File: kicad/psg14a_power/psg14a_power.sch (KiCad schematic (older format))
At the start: 5 parts

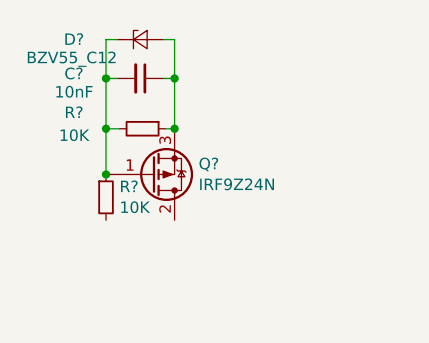
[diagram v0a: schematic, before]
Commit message: [psg14a_power]Schematics finished
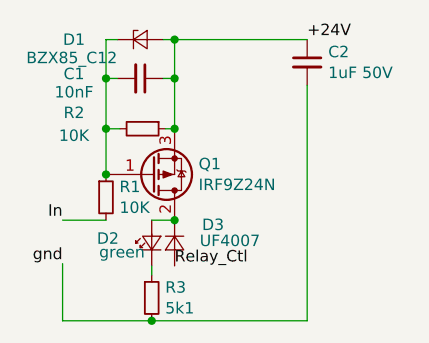
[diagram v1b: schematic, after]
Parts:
- added C2: 1uF 50V, Capacitors_SMD:C_0805_HandSoldering, symbol Device:C_Small
- added D2: green, LEDs:LED_0805_HandSoldering, symbol Device:LED_Small
- added D3: UF4007, Diodes_THT:D_DO-41_SOD81_P5.08mm_Vertical_AnodeUp, symbol Device:D_Small
- added R3: 5k1, Resistors_SMD:R_0805_HandSoldering, symbol Device:R_Small
- C1: renamed from C?; footprint (none) -> Capacitors_SMD:C_0805_HandSoldering
- D1: renamed from D?; value BZV55_C12 -> BZX85_C12; footprint (none) -> Diodes_THT:D_DO-41_SOD81_P5.08mm_Vertical_AnodeUp
- Q1: renamed from Q?; footprint Package_TO_SOT_THT:TO-220-3_Vertical -> TO_SOT_Packages_THT:TO-220-3_Vertical
- R1, R2: renamed from R?; footprint (none) -> Resistors_SMD:R_0805_HandSoldering
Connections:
- net at Q1.2 (D): now also D2.2 (A), D3.1 (K)
- net +24V: now reaches C1.1, D1.2 (A), Q1.3 (S), R2.1
- net +24V: now also C2.1
- net In: now reaches R1.2
- new net: D2.1 (K), R3.1
- new net Relay_Ctl: D3.2 (A)
- new net gnd: C2.2, R3.2
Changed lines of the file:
@@
 EESchema Schematic File Version 4
+LIBS:psg14a_power-cache
 EELAYER 26 0
 EELAYER END
@@
 $EndDescr
 $Comp
-L Transistor_FET:IRF9540N Q?
+L Transistor_FET:IRF9540N Q1
 U 1 1 5C02A0F2
 P 2450 1430
-F 0 "Q?" H 2655 1384 50  0000 L CNN
+F 0 "Q1" H 2655 1384 50  0000 L CNN
 F 1 "IRF9Z24N" H 2655 1475 50  0000 L CNN
-F 2 "Package_TO_SOT_THT:TO-220-3_Vertical" H 2650 1355 50  0001 L CIN
+F 2 "TO_SOT_Packages_THT:TO-220-3_Vertical" H 2650 1355 50  0001 L CIN
 F 3 "http://www.irf.com/product-info/datasheets/data/irf9540n.pdf" H 2450 1430 50  0001 L CNN
 	1    2450 1430
@@
 $EndComp
 $Comp
-L Device:R_Small R?
+L Device:R_Small R1
 U 1 1 5C02A204
 P 2250 1530
-F 0 "R?" H 2309 1576 50  0000 L CNN
+F 0 "R1" H 2309 1576 50  0000 L CNN
 F 1 "10K" H 2309 1485 50  0000 L CNN
-F 2 "" H 2250 1530 50  0001 C CNN
+F 2 "Resistors_SMD:R_0805_HandSoldering" H 2250 1530 50  0001 C CNN
 F 3 "~" H 2250 1530 50  0001 C CNN
 	1    2250 1530
@@
 $EndComp
 $Comp
-L Device:R_Small R?
+L Device:R_Small R2
 U 1 1 5C02A2A6
 P 2410 1230
-F 0 "R?" V 2340 930 50  0000 C CNN
+F 0 "R2" V 2340 930 50  0000 C CNN
 F 1 "10K" V 2440 930 50  0000 C CNN
-F 2 "" H 2410 1230 50  0001 C CNN
+F 2 "Resistors_SMD:R_0805_HandSoldering" H 2410 1230 50  0001 C CNN
 F 3 "~" H 2410 1230 50  0001 C CNN
 	1    2410 1230
@@
 Connection ~ 2250 1430
 $Comp
-L Device:C_Small C?
+L Device:C_Small C1
 U 1 1 5C02A3CA
 P 2400 1010
-F 0 "C?" V 2380 720 50  0000 C CNN
+F 0 "C1" V 2380 720 50  0000 C CNN
 F 1 "10nF" V 2460 720 50  0000 C CNN
-F 2 "" H 2400 1010 50  0001 C CNN
+F 2 "Capacitors_SMD:C_0805_HandSoldering" H 2400 1010 50  0001 C CNN
 F 3 "~" H 2400 1010 50  0001 C CNN
 	1    2400 1010
@@
 $EndComp
 $Comp
-L Device:D_Zener_Small D?
+L Device:D_Zener_Small D1
 U 1 1 5C02A910
 P 2400 840
-F 0 "D?" H 2110 840 50  0000 C CNN
-F 1 "BZV55_C12" H 2100 760 50  0000 C CNN
-F 2 "" V 2400 840 50  0001 C CNN
+F 0 "D1" H 2110 840 50  0000 C CNN
+F 1 "BZX85_C12" H 2100 760 50  0000 C CNN
+F 2 "Diodes_THT:D_DO-41_SOD81_P5.08mm_Vertical_AnodeUp" V 2400 840 50  0001 C CNN
 F 3 "~" V 2400 840 50  0001 C CNN
 	1    2400 840
@@
 Wire Wire Line
 	2250 1230 2250 1430
+Wire Wire Line
+	2250 1630 2060 1630
+Text Label 2060 1630 2    50   ~ 0
+In
+$Comp
+L Device:D_Small D3
+U 1 1 5C0EF074
+P 2550 1730
+F 0 "D3" V 2470 1850 50  0000 L CNN
+F 1 "UF4007" V 2540 1840 50  0000 L CNN
+F 2 "Diodes_THT:D_DO-41_SOD81_P5.08mm_Vertical_AnodeUp" V 2550 1730 50  0001 C CNN
+F 3 "~" V 2550 1730 50  0001 C CNN
+	1    2550 1730
+	0    1    1    0
+$EndComp
+Wire Wire Line
+	2550 1630 2450 1630
+$Comp
+L Device:LED_Small D2
+U 1 1 5C0EF3AD
+P 2450 1730
+F 0 "D2" V 2470 1970 50  0000 R CNN
+F 1 "green" V 2410 1960 50  0000 R CNN
+F 2 "LEDs:LED_0805_HandSoldering" V 2450 1730 50  0001 C CNN
+F 3 "~" V 2450 1730 50  0001 C CNN
+	1    2450 1730
+	0    -1   -1   0
+$EndComp
+Connection ~ 2550 1630
+$Comp
+L Device:R_Small R3
+U 1 1 5C0EF5C4
+P 2450 1970
+F 0 "R3" H 2509 2016 50  0000 L CNN
+F 1 "5k1" H 2509 1925 50  0000 L CNN
+F 2 "Resistors_SMD:R_0805_HandSoldering" H 2450 1970 50  0001 C CNN
+F 3 "~" H 2450 1970 50  0001 C CNN
+	1    2450 1970
+	1    0    0    -1
+$EndComp
+Wire Wire Line
+	2450 1830 2450 1870
+Text Label 2550 1830 0    50   ~ 0
+Relay_Ctl
+Wire Wire Line
+	2060 1820 2060 2070
+Wire Wire Line
+	2060 2070 2450 2070
+Connection ~ 2450 2070
+Wire Wire Line
+	2450 2070 3130 2070
+$Comp
+L Device:C_Small C2
+U 1 1 5C0EFE1A
+P 3130 940
+F 0 "C2" H 3222 986 50  0000 L CNN
+F 1 "1uF 50V" H 3222 895 50  0000 L CNN
+F 2 "Capacitors_SMD:C_0805_HandSoldering" H 3130 940 50  0001 C CNN
+F 3 "~" H 3130 940 50  0001 C CNN
+	1    3130 940
+	1    0    0    -1
+$EndComp
+Wire Wire Line
+	3130 1040 3130 2070
+Wire Wire Line
+	3130 840  2550 840
+Connection ~ 2550 840
+Text Label 2060 1820 2    50   ~ 0
+gnd
+Text Label 3130 840  0    50   ~ 0
++24V
 $EndSCHEMATC

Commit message: [psg14a] looking how to copy blocks
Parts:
- added C10, C5, C6, C8: 1uF 50V, Capacitors_SMD:C_0805_HandSoldering, symbol Device:C_Small
- added C3, C4, C7, C9: 10nF, Capacitors_SMD:C_0805_HandSoldering, symbol Device:C_Small
- added D10, D13, D4, D5: BZX85_C12, Diodes_THT:D_DO-41_SOD81_P5.08mm_Vertical_AnodeUp, symbol Device:D_Zener_Small
- added D11, D14, D6, D7: green, LEDs:LED_0805_HandSoldering, symbol Device:LED_Small
- added D12, D15, D8, D9: UF4007, Diodes_THT:D_DO-41_SOD81_P5.08mm_Vertical_AnodeUp, symbol Device:D_Small
- added Q2, Q3, Q4, Q5: IRF9Z24N, TO_SOT_Packages_THT:TO-220-3_Vertical, symbol Transistor_FET:IRF9540N
- added R10, R11, R13, R14, R4, R5, R6, R8: 10K, Resistors_SMD:R_0805_HandSoldering, symbol Device:R_Small
- added R12, R15, R7, R9: 5k1, Resistors_SMD:R_0805_HandSoldering, symbol Device:R_Small
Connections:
- net +24V: now also C10.1, C3.1, C4.1, C5.1, C6.1, C7.1, C8.1, C9.1, D10.2 (A), D13.2 (A), D4.2 (A), D5.2 (A), Q2.3 (S), Q3.3 (S), Q4.3 (S), Q5.3 (S), R11.1, R14.1, R6.1, R8.1
- net In: now also R10.2, R13.2, R4.2, R5.2
- net Relay_Ctl: now also D2.2 (A), D3.1 (K), Q1.2 (D), D11.2 (A), D12.1 (K), D14.2 (A), D15.1 (K), D6.2 (A), D7.2 (A), D8.1 (K), D9.1 (K), Q2.2 (D), Q3.2 (D), Q4.2 (D), Q5.2 (D); no longer D3.2 (A)
- net gnd: now also C10.2, C5.2, C6.2, C8.2, D12.2 (A), D8.2 (A), D9.2 (A), R12.2, R15.2, R7.2, R9.2
- new net: C9.2, D13.1 (K), Q5.1 (G), R13.1, R14.2
- new net: D14.1 (K), R15.1
- new net: C3.2, D4.1 (K), Q2.1 (G), R4.1, R6.2
- new net: D6.1 (K), R7.1
- new net: C4.2, D5.1 (K), Q3.1 (G), R5.1, R8.2
- new net: D7.1 (K), R9.1
- new net: C7.2, D10.1 (K), Q4.1 (G), R10.1, R11.2
- new net: D11.1 (K), R12.1

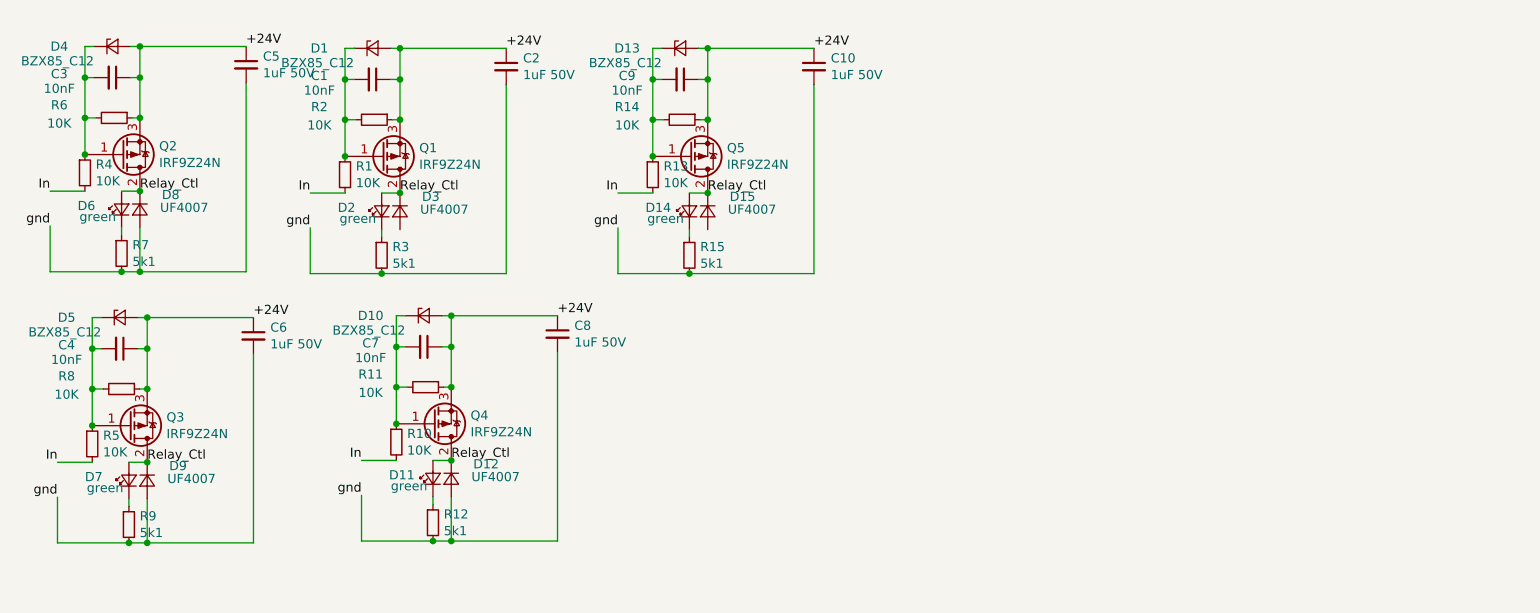
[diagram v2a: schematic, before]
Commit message: [psg14a_power]New route added
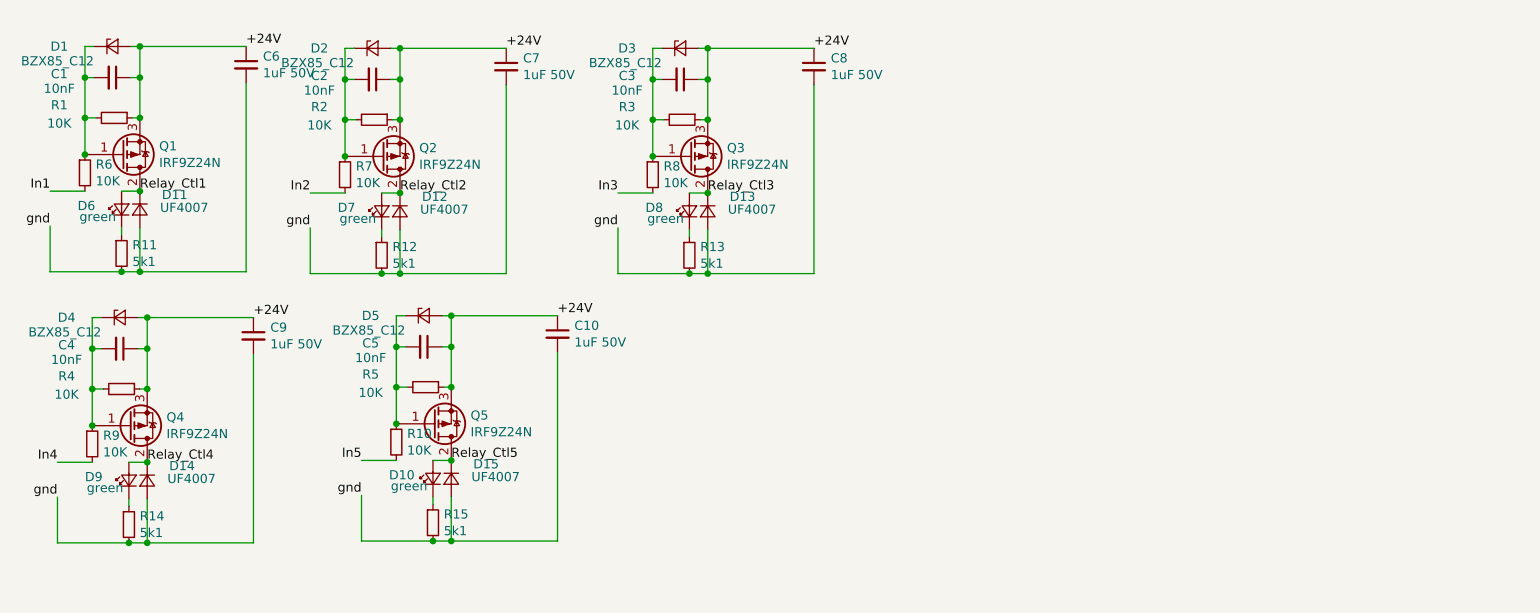
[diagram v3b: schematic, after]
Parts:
- renumbered C3 to C1, C8 to C10, C1 to C2, C9 to C3, C7 to C5, C5 to C6, C2 to C7, C10 to C8, C6 to C9, D4 to D1, D11 to D10, D8 to D11, D3 to D12, D15 to D13, D9 to D14, D12 to D15, D1 to D2, D13 to D3, D5 to D4, D10 to D5, D2 to D7, D14 to D8, D7 to D9, Q2 to Q1, Q1 to Q2, Q5 to Q3, Q3 to Q4, Q4 to Q5, R6 to R1, R7 to R11, R3 to R12, R15 to R13, R9 to R14, R12 to R15, R14 to R3, R8 to R4, R11 to R5, R4 to R6, R1 to R7, R13 to R8, R5 to R9
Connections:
- net gnd: now also D12.2 (A), D13.2 (A)
- removed net In: R10.2, R6.2, R7.2, R8.2, R9.2
- removed net Relay_Ctl: D10.2 (A), D11.1 (K), D12.1 (K), D13.1 (K), D14.1 (K), D15.1 (K), D6.2 (A), D7.2 (A), D8.2 (A), D9.2 (A), Q1.2 (D), Q2.2 (D), Q3.2 (D), Q4.2 (D), Q5.2 (D)
- new net In1: R6.2
- new net In2: R7.2
- new net In3: R8.2
- new net In4: R9.2
- new net In5: R10.2
- new net Relay_Ctl1: D11.1 (K), D6.2 (A), Q1.2 (D)
- new net Relay_Ctl2: D12.1 (K), D7.2 (A), Q2.2 (D)
- new net Relay_Ctl3: D13.1 (K), D8.2 (A), Q3.2 (D)
- new net Relay_Ctl4: D14.1 (K), D9.2 (A), Q4.2 (D)
- new net Relay_Ctl5: D10.2 (A), D15.1 (K), Q5.2 (D)

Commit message: [psg14a_power] Switch to multiple sheets layout
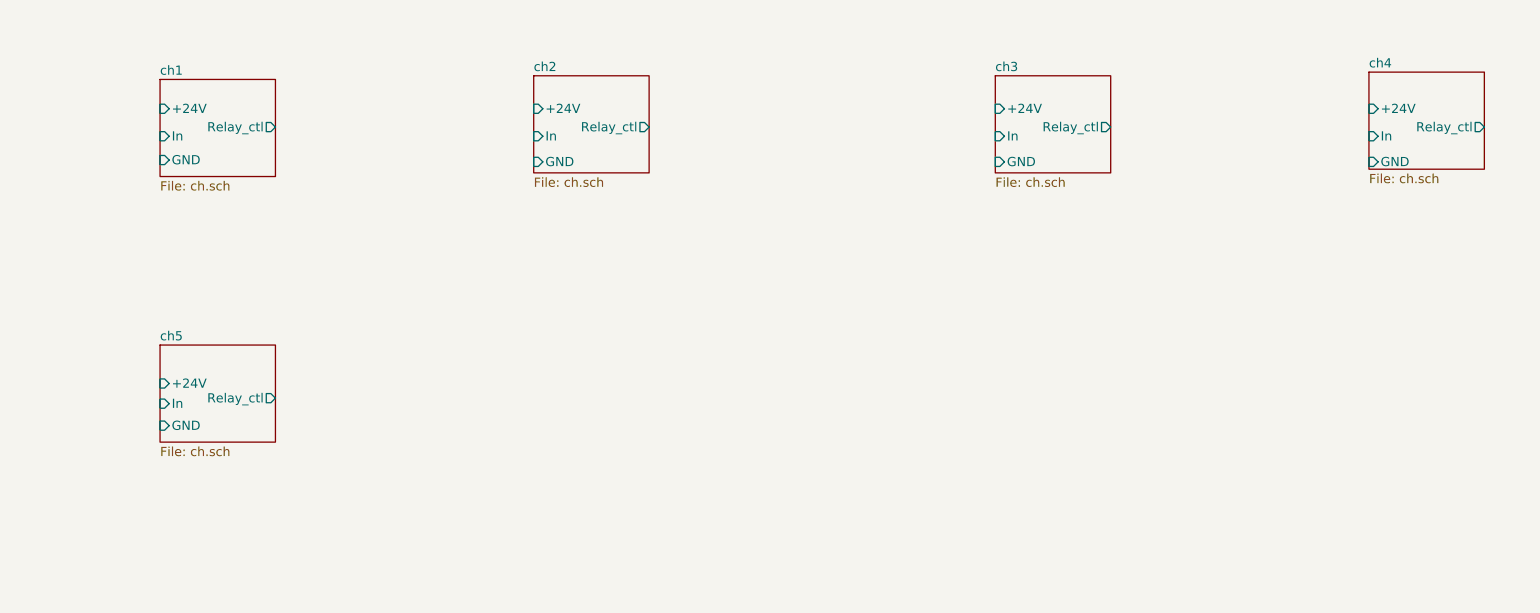
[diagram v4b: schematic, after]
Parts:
- removed C1, C2, C3, C4, C5: 10nF, Capacitors_SMD:C_0805_HandSoldering, symbol Device:C_Small
- removed C10, C6, C7, C8, C9: 1uF 50V, Capacitors_SMD:C_0805_HandSoldering, symbol Device:C_Small
- removed D1, D2, D3, D4, D5: BZX85_C12, Diodes_THT:D_DO-41_SOD81_P5.08mm_Vertical_AnodeUp, symbol Device:D_Zener_Small
- removed D10, D6, D7, D8, D9: green, LEDs:LED_0805_HandSoldering, symbol Device:LED_Small
- removed D11, D12, D13, D14, D15: UF4007, Diodes_THT:D_DO-41_SOD81_P5.08mm_Vertical_AnodeUp, symbol Device:D_Small
- removed Q1, Q2, Q3, Q4, Q5: IRF9Z24N, TO_SOT_Packages_THT:TO-220-3_Vertical, symbol Transistor_FET:IRF9540N
- removed R1, R10, R2, R3, R4, R5, R6, R7, R8, R9: 10K, Resistors_SMD:R_0805_HandSoldering, symbol Device:R_Small
- removed R11, R12, R13, R14, R15: 5k1, Resistors_SMD:R_0805_HandSoldering, symbol Device:R_Small

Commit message: [psg14a_power] Ready for replication which does not work ;-)
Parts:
- added J1: Power, TerminalBlocks_Phoenix:TerminalBlock_Phoenix_MPT-2.54mm_2pol, symbol Connector:Screw_Terminal_01x02
- added J2: In, TerminalBlocks_Phoenix:TerminalBlock_Phoenix_MPT-2.54mm_6pol, symbol Connector_Generic:Conn_01x06
- added J3: Out, TerminalBlocks_Phoenix:TerminalBlock_Phoenix_MPT-2.54mm_6pol, symbol Connector_Generic:Conn_01x06
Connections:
- new net +24V: J1.2 (Pin_2)
- new net GND: J1.1 (Pin_1), J2.6 (Pin_6), J3.6 (Pin_6)
- new net In1: J2.1 (Pin_1)
- new net In2: J2.2 (Pin_2)
- new net In3: J2.3 (Pin_3)
- new net In4: J2.4 (Pin_4)
- new net In5: J2.5 (Pin_5)
- new net Out1: J3.1 (Pin_1)
- new net Out2: J3.2 (Pin_2)
- new net Out3: J3.3 (Pin_3)
- new net Out4: J3.4 (Pin_4)
- new net Out5: J3.5 (Pin_5)
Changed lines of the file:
@@
 F5 "Relay_ctl" O R 1870 2750 50
 $EndSheet
+Wire Wire Line
+	1240 1450 1180 1450
+Wire Wire Line
+	1180 1450 1180 1640
+Wire Wire Line
+	1180 2900 1240 2900
+Wire Wire Line
+	1180 1640 3230 1640
+Wire Wire Line
+	7800 1640 7800 1460
+Wire Wire Line
+	7800 1460 7840 1460
+Connection ~ 1180 1640
+Wire Wire Line
+	1180 1640 1180 2900
+Wire Wire Line
+	3280 1460 3230 1460
+Wire Wire Line
+	3230 1460 3230 1640
+Connection ~ 3230 1640
+Wire Wire Line
+	3230 1640 5770 1640
+Wire Wire Line
+	5800 1460 5770 1460
+Wire Wire Line
+	5770 1460 5770 1640
+Connection ~ 5770 1640
+Wire Wire Line
+	5770 1640 7800 1640
+Wire Wire Line
+	1240 1170 1120 1170
+Wire Wire Line
+	1120 1170 1120 2670
+Wire Wire Line
+	1120 2670 1240 2670
+Wire Wire Line
+	1120 1170 1120 890
+Wire Wire Line
+	1120 890  3230 890
+Wire Wire Line
+	7810 890  7810 1170
+Wire Wire Line
+	7810 1170 7840 1170
+Connection ~ 1120 1170
+Wire Wire Line
+	5800 1170 5770 1170
+Wire Wire Line
+	5770 1170 5770 890
+Connection ~ 5770 890
+Wire Wire Line
+	5770 890  7810 890
+Wire Wire Line
+	3280 1170 3230 1170
+Wire Wire Line
+	3230 1170 3230 890
+Connection ~ 3230 890
+Wire Wire Line
+	3230 890  5770 890
+Text Label 3230 1640 3    50   ~ 0
+GND
+Text Label 3240 890  1    50   ~ 0
++24V
+Text Label 1240 1320 2    50   ~ 0
+In1
+Text Label 3280 1320 2    50   ~ 0
+In2
+Text Label 5800 1320 2    50   ~ 0
+In3
+Text Label 7840 1320 2    50   ~ 0
+In4
+Text Label 1240 2780 2    50   ~ 0
+In5
+Text Label 1870 1270 0    50   ~ 0
+Out1
+Text Label 3910 1270 0    50   ~ 0
+Out2
+Text Label 6430 1270 0    50   ~ 0
+Out3
+Text Label 8470 1270 0    50   ~ 0
+Out4
+Text Label 1870 2750 0    50   ~ 0
+Out5
+$Comp
+L Connector:Screw_Terminal_01x02 J1
+U 1 1 5C183449
+P 1450 3770
+F 0 "J1" H 1370 3445 50  0000 C CNN
+F 1 "Power" H 1370 3536 50  0000 C CNN
+F 2 "TerminalBlocks_Phoenix:TerminalBlock_Phoenix_MPT-2.54mm_2pol" H 1450 3770 50  0001 C CNN
+F 3 "~" H 1450 3770 50  0001 C CNN
+	1    1450 3770
+	-1   0    0    1
+$EndComp
+Text Label 1650 3770 0    50   ~ 0
+GND
+Text Label 1650 3670 0    50   ~ 0
++24V
+$Comp
+L Connector_Generic:Conn_01x06 J2
+U 1 1 5C183BBE
+P 2450 3490
+F 0 "J2" H 2530 3482 50  0000 L CNN
+F 1 "In" H 2530 3391 50  0000 L CNN
+F 2 "TerminalBlocks_Phoenix:TerminalBlock_Phoenix_MPT-2.54mm_6pol" H 2450 3490 50  0001 C CNN
+F 3 "~" H 2450 3490 50  0001 C CNN
+	1    2450 3490
+	1    0    0    -1
+$EndComp
+Text Label 2250 3790 2    50   ~ 0
+GND
+Text Label 2250 3290 2    50   ~ 0
+In1
+Text Label 2250 3390 2    50   ~ 0
+In2
+Text Label 2250 3490 2    50   ~ 0
+In3
+Text Label 2250 3590 2    50   ~ 0
+In4
+Text Label 2250 3690 2    50   ~ 0
+In5
+$Comp
+L Connector_Generic:Conn_01x06 J3
+U 1 1 5C183D59
+P 3080 3480
+F 0 "J3" H 3159 3472 50  0000 L CNN
+F 1 "Out" H 3159 3381 50  0000 L CNN
+F 2 "TerminalBlocks_Phoenix:TerminalBlock_Phoenix_MPT-2.54mm_6pol" H 3080 3480 50  0001 C CNN
+F 3 "~" H 3080 3480 50  0001 C CNN
+	1    3080 3480
+	1    0    0    -1
+$EndComp
+Text Label 2880 3780 2    50   ~ 0
+GND
+Text Label 2880 3280 2    50   ~ 0
+Out1
+Text Label 2880 3380 2    50   ~ 0
+Out2
+Text Label 2880 3480 2    50   ~ 0
+Out3
+Text Label 2880 3580 2    50   ~ 0
+Out4
+Text Label 2880 3680 2    50   ~ 0
+Out5
 $EndSCHEMATC

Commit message: [psg14a_power]Ready for review by Ioan the Greatest
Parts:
- added D16: green, LEDs:LED_0805_HandSoldering, symbol Device:LED_Small
- added H1, H2, H3: Mech, Mounting_Holes:MountingHole_3.2mm_M3, symbol Mechanical:MountingHole
- added R16: 5K1, Resistors_SMD:R_0805_HandSoldering, symbol Device:R_Small
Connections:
- net +24V: now also D16.2 (A)
- net GND: now also R16.2
- new net: D16.1 (K), R16.1
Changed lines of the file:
@@
 Text Label 2880 3680 2    50   ~ 0
 Out5
+$Comp
+L Device:R_Small R16
+U 1 1 5C1D8B10
+P 2740 2620
+F 0 "R16" H 2799 2666 50  0000 L CNN
+F 1 "5K1" H 2799 2575 50  0000 L CNN
+F 2 "Resistors_SMD:R_0805_HandSoldering" H 2740 2620 50  0001 C CNN
+F 3 "~" H 2740 2620 50  0001 C CNN
+	1    2740 2620
+	1    0    0    -1
+$EndComp
+$Comp
+L Device:LED_Small D16
+U 1 1 5C1D8DFC
+P 2740 2420
+F 0 "D16" V 2786 2352 50  0000 R CNN
+F 1 "green" V 2695 2352 50  0000 R CNN
+F 2 "LEDs:LED_0805_HandSoldering" V 2740 2420 50  0001 C CNN
+F 3 "~" V 2740 2420 50  0001 C CNN
+	1    2740 2420
+	0    -1   -1   0
+$EndComp
+Text Label 2740 2320 0    50   ~ 0
++24V
+Text Label 2740 2720 2    50   ~ 0
+GND
+$Comp
+L Mechanical:MountingHole H1
+U 1 1 5C1D9BBE
+P 2280 2910
+F 0 "H1" H 2380 2956 50  0000 L CNN
+F 1 "Mech" H 2380 2865 50  0000 L CNN
+F 2 "Mounting_Holes:MountingHole_3.2mm_M3" H 2280 2910 50  0001 C CNN
+F 3 "~" H 2280 2910 50  0001 C CNN
+	1    2280 2910
+	1    0    0    -1
+$EndComp
+$Comp
+L Mechanical:MountingHole H2
+U 1 1 5C1D9C5A
+P 2560 2920
+F 0 "H2" H 2660 2966 50  0000 L CNN
+F 1 "Mech" H 2660 2875 50  0000 L CNN
+F 2 "Mounting_Holes:MountingHole_3.2mm_M3" H 2560 2920 50  0001 C CNN
+F 3 "~" H 2560 2920 50  0001 C CNN
+	1    2560 2920
+	1    0    0    -1
+$EndComp
+$Comp
+L Mechanical:MountingHole H3
+U 1 1 5C1D9CE6
+P 2850 2920
+F 0 "H3" H 2950 2966 50  0000 L CNN
+F 1 "Mech" H 2950 2875 50  0000 L CNN
+F 2 "Mounting_Holes:MountingHole_3.2mm_M3" H 2850 2920 50  0001 C CNN
+F 3 "~" H 2850 2920 50  0001 C CNN
+	1    2850 2920
+	1    0    0    -1
+$EndComp
 $EndSCHEMATC

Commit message: [Psg14a_power] Ioan the Greatest was drunk. Ready for production
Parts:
- J1: footprint TerminalBlocks_Phoenix:TerminalBlock_Phoenix_MPT-2.54mm_2pol -> TerminalBlocks_Phoenix:TerminalBlock_Phoenix_PT-3.5mm_2pol
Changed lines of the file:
@@
 F 0 "J1" H 1370 3445 50  0000 C CNN
 F 1 "Power" H 1370 3536 50  0000 C CNN
-F 2 "TerminalBlocks_Phoenix:TerminalBlock_Phoenix_MPT-2.54mm_2pol" H 1450 3770 50  0001 C CNN
+F 2 "TerminalBlocks_Phoenix:TerminalBlock_Phoenix_PT-3.5mm_2pol" H 1450 3770 50  0001 C CNN
 F 3 "~" H 1450 3770 50  0001 C CNN
 	1    1450 3770
